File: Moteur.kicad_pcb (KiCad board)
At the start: 4 copper layers, 31.8 x 16 mm, 53 parts, among them IC1 TPS71501, IC2 TLV710, IC3 MAX3051, IC4 LM5106, IC5 LM5106, IC6 INA282, P1 Bus2, P2 CONN_6, P3 GPIO, P4 CONN_1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

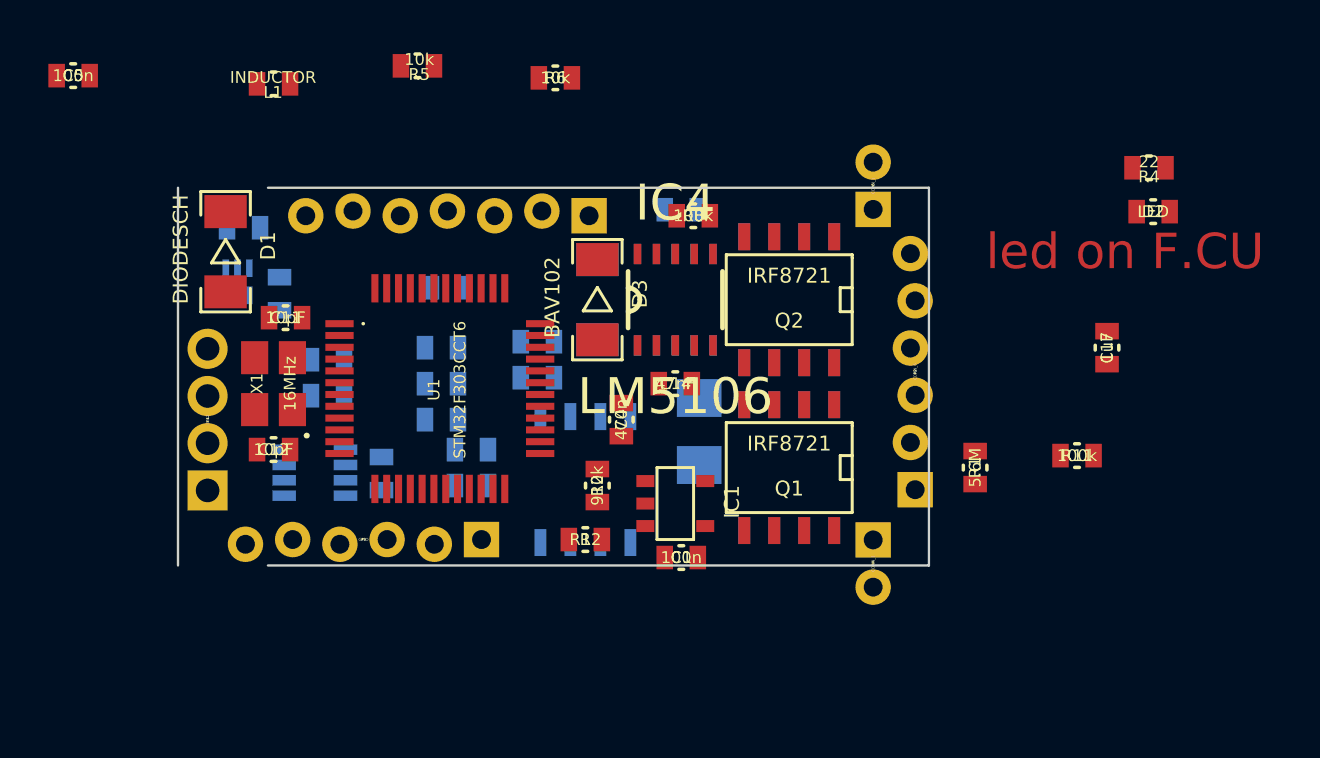
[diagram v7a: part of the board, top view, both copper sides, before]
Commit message: component placement
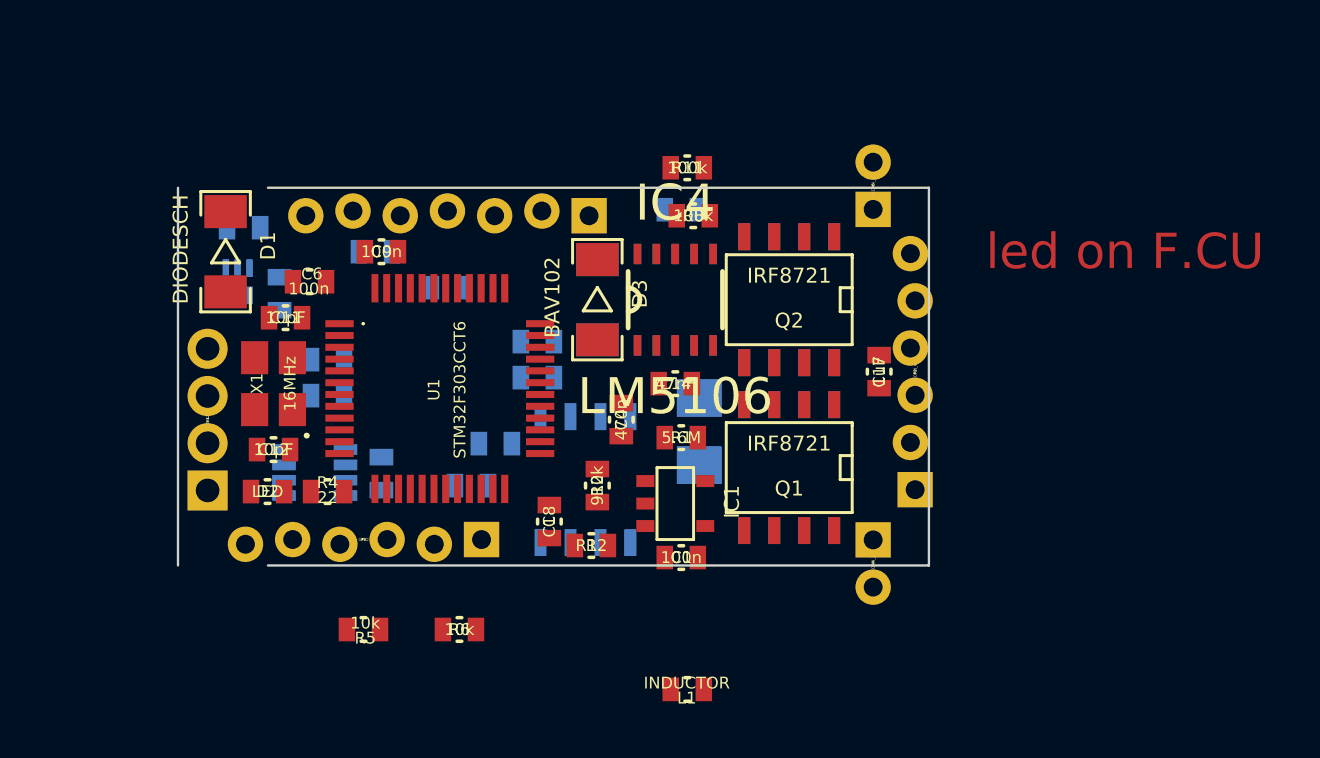
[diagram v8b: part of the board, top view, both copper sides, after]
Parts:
- C18, C6, C9: moved to F.Cu
- C5: moved to B.Cu
- moved D2 39.3 mm to (126.0, 102.9)
- moved R4 37.4 mm to (128.5, 102.9), turned to 180 degrees
- moved L1 31.1 mm to (143.8, 111.3)
- moved R5 24.0 mm to (130.0, 108.7)
- moved R6 23.7 mm to (134.1, 108.7)
- moved R11 20.5 mm to (143.8, 89.2)
- moved C5 14.8 mm to (130.6, 92.7), turned to 180 degrees
- moved R1 12.5 mm to (143.5, 100.6), turned to 180 degrees
- moved C17 9.71 mm to (151.9, 97.8)
- moved C6 7.06 mm to (127.8, 94.0), turned to 180 degrees
- moved C9 4.79 mm to (130.8, 92.7)
- moved C18 4.49 mm to (137.9, 104.1), turned to 90 degrees
- moved C7 2.50 mm to (135.6, 100.8), turned to 180 degrees
- moved R12 0.36 mm to (139.7, 105.2)
